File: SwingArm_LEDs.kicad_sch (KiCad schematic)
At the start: 42 parts, among them U1 ICM7555xB

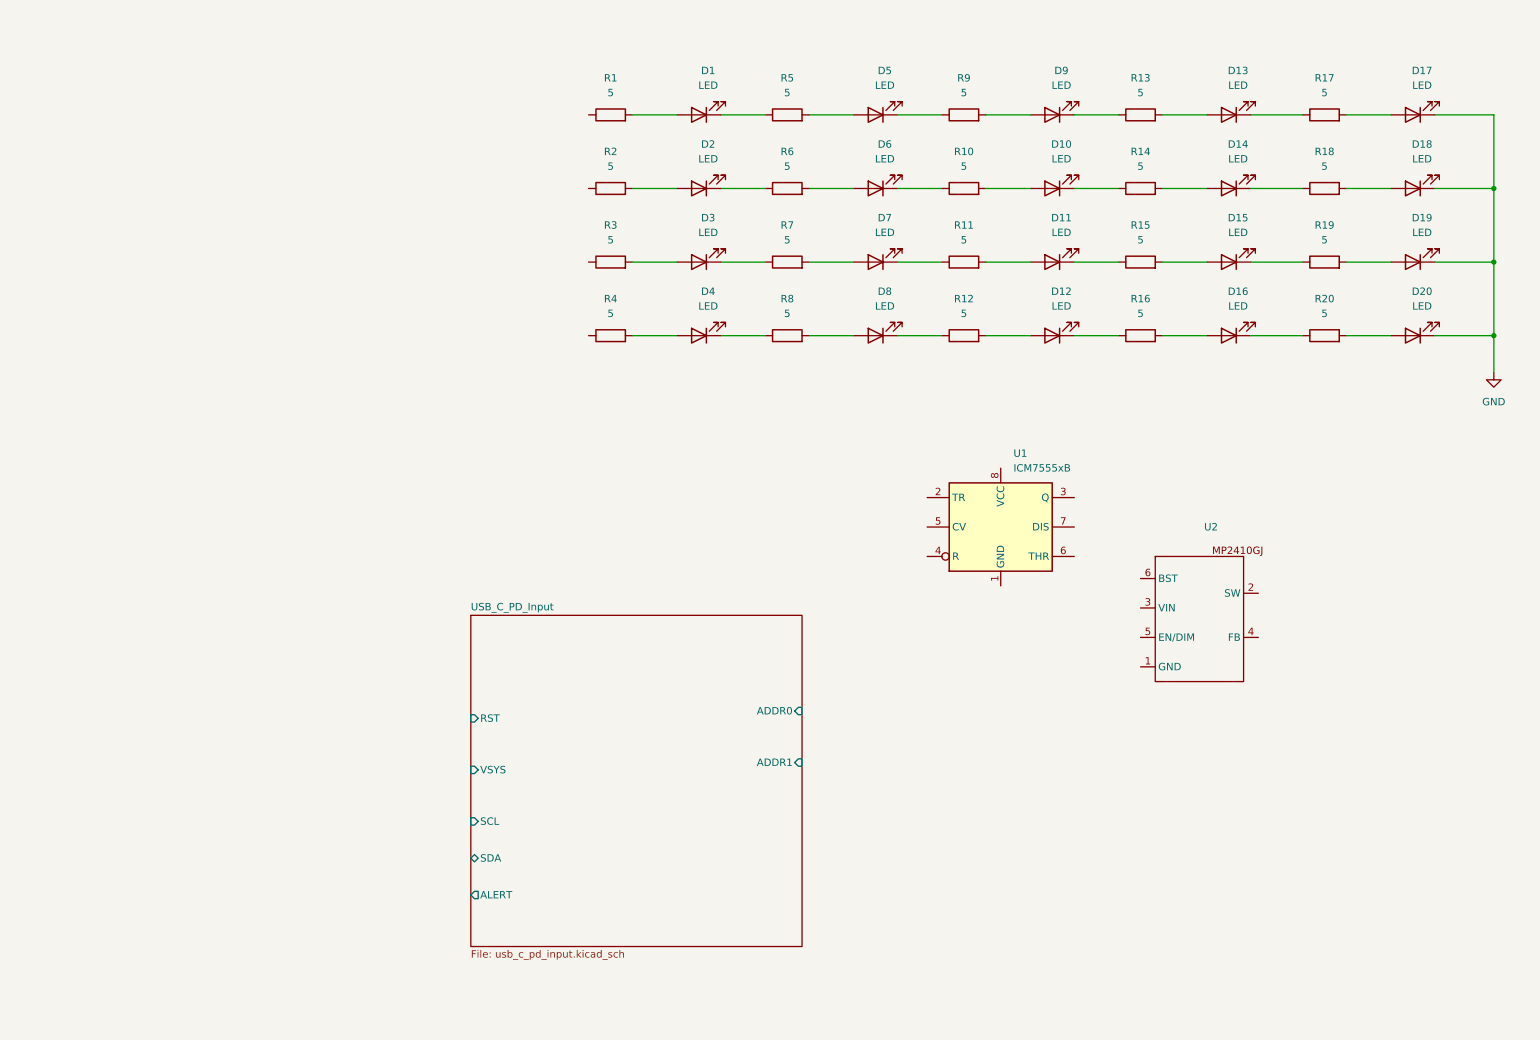
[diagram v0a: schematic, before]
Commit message: Add usb c power + led driver
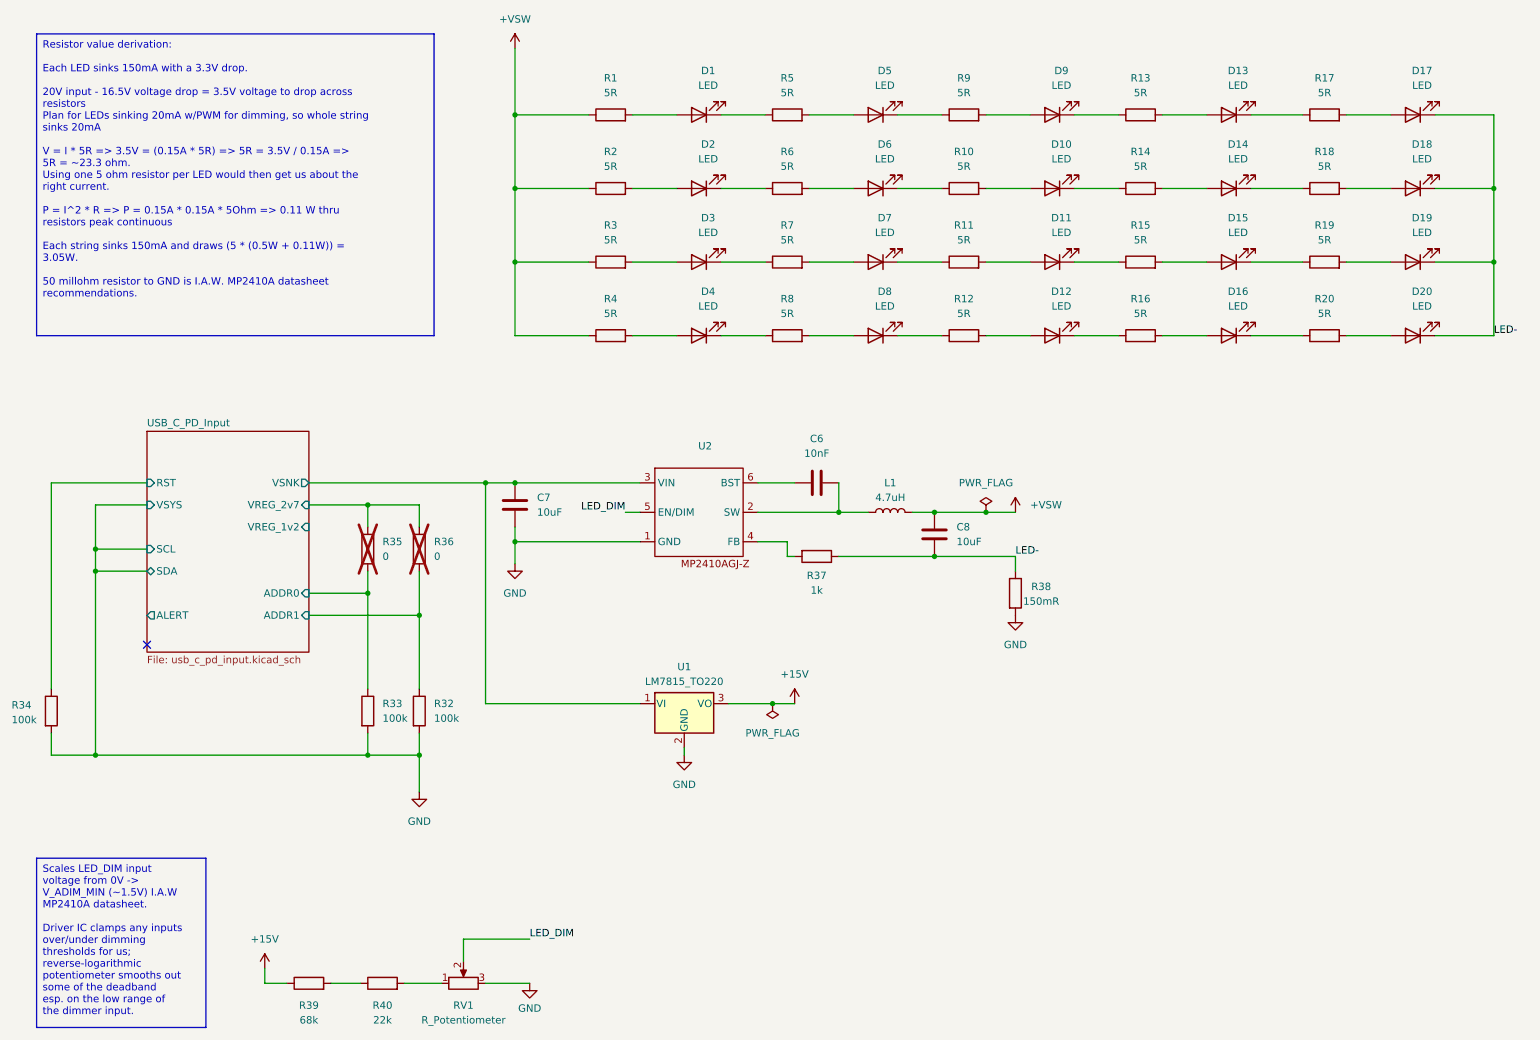
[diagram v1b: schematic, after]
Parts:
- removed U1: ICM7555xB, Package_SO:SOIC-8_3.9x4.9mm_P1.27mm, symbol Timer:ICM7555xB
- removed U2: ~, Package_TO_SOT_SMD:TSOT-23-6_HandSoldering, symbol ASethi_Parts:MP2410GJ
- added C6: 10nF, symbol Device:C
- added C7, C8: 10uF, symbol Device:C
- added L1: 4.7uH, symbol Device:L
- added R32, R33, R34: 100k, symbol Device:R
- added R35, R36: 0, symbol Device:R
- added R37: 1k, symbol Device:R
- added R38: 150mR, symbol Device:R
- added R39: 68k, symbol Device:R
- added R40: 22k, symbol Device:R
- added RV1: R_Potentiometer, symbol Device:R_Potentiometer
- added U1: LM7815_TO220, Package_TO_SOT_THT:TO-220-3_Vertical, symbol Regulator_Linear:LM7815_TO220
- added U2: ~, Package_TO_SOT_SMD:TSOT-23-6_HandSoldering, symbol ASethi_Parts:MP2410AGJ
- D1, D10, D11, D12, D13, D14, D15, D16, D17, D18, D19, D2, D20, D3, D4, D5, D6, D7, D8, D9: footprint (none) -> LED_SMD:LED_PLCC_2835_Handsoldering
- R1, R10, R11, R12, R13, R14, R15, R16, R17, R18, R19, R2, R20, R3, R4, R5, R6, R7, R8, R9: value 5 -> 5R; footprint (none) -> Resistor_SMD:R_0805_2012Metric
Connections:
- net GND: now also C7.1, R32.2, R33.2, R34.2, R38.2, RV1.3, U1.2 (GND), U2.1 (GND); no longer D17.1 (K), D18.1 (K), D19.1 (K), D20.1 (K)
- net USB_C_PD_Input/ADDR0: now also R33.1, R35.2
- net USB_C_PD_Input/ADDR1: now also R32.1, R36.2
- net USB_C_PD_Input/RST: now also R34.1
- net +VSW: now reaches R4.1
- net +VSW: now also R1.1, R2.1, R3.1, C8.2, L1.2
- new net: R39.2, R40.1
- new net: R40.2, RV1.1
- new net: C6.1, U2.6 (BST)
- new net: C6.2, L1.1, U2.2 (SW)
- new net: R37.2, U2.4 (FB)
- new net +15V: R39.1, U1.3 (VO)
- new net LED-: C8.1, D17.1 (K), D18.1 (K), D19.1 (K), D20.1 (K), R37.1, R38.1
- new net LED_DIM: RV1.2, U2.5 (EN/DIM)
- new net USB_C_PD_Input/VREG_2v7: R35.1, R36.1
- new net USB_C_PD_Input/VSNK: C7.2, U1.1 (VI), U2.3 (VIN)
- no-connect marks 0 -> 1
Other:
- sheet USB_C_PD_Input ports: added VREG_1v2, VREG_2v7, VSNK; removed none

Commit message: Fix ERC
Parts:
- C6, C8: footprint (none) -> Capacitor_SMD:C_0805_2012Metric_Pad1.18x1.45mm_HandSolder
- C7: value 10uF -> C; footprint (none) -> Capacitor_SMD:C_0805_2012Metric_Pad1.18x1.45mm_HandSolder
- L1: footprint (none) -> Inductor_SMD:L_0805_2012Metric_Pad1.15x1.40mm_HandSolder
- R1, R10, R11, R12, R13, R14, R15, R16, R17, R18, R19, R2, R20, R3, R4, R5, R6, R7, R8, R9: footprint Resistor_SMD:R_0805_2012Metric -> Resistor_SMD:R_0805_2012Metric_Pad1.20x1.40mm_HandSolder
- R32, R33, R34, R37, R38, R39, R40: footprint (none) -> Resistor_SMD:R_0805_2012Metric_Pad1.20x1.40mm_HandSolder
- R35, R36: value 0 -> R; footprint (none) -> Resistor_SMD:R_0805_2012Metric_Pad1.20x1.40mm_HandSolder
- RV1: footprint (none) -> ASethi_Footprints:PDB181_K420F_103C; Mfr. Name (none) -> Bourns; Mfr. Part Number (none) -> PDB181-K420F-103C
- U2: value ~ -> MP2410AG-Z
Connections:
- net +VSW renamed LED+
- no-connect marks 1 -> 2
